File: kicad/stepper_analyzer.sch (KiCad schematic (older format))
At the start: 22 parts, among them J1 Connector_Conn_01x04_Male, J2 Connector_Conn_01x04_Male, M1 Motor, Q1 AO3400A, U1 ACS70331EOLCTR-2P5B3, U2 ACS70331EOLCTR-2P5B3, U3 Pico

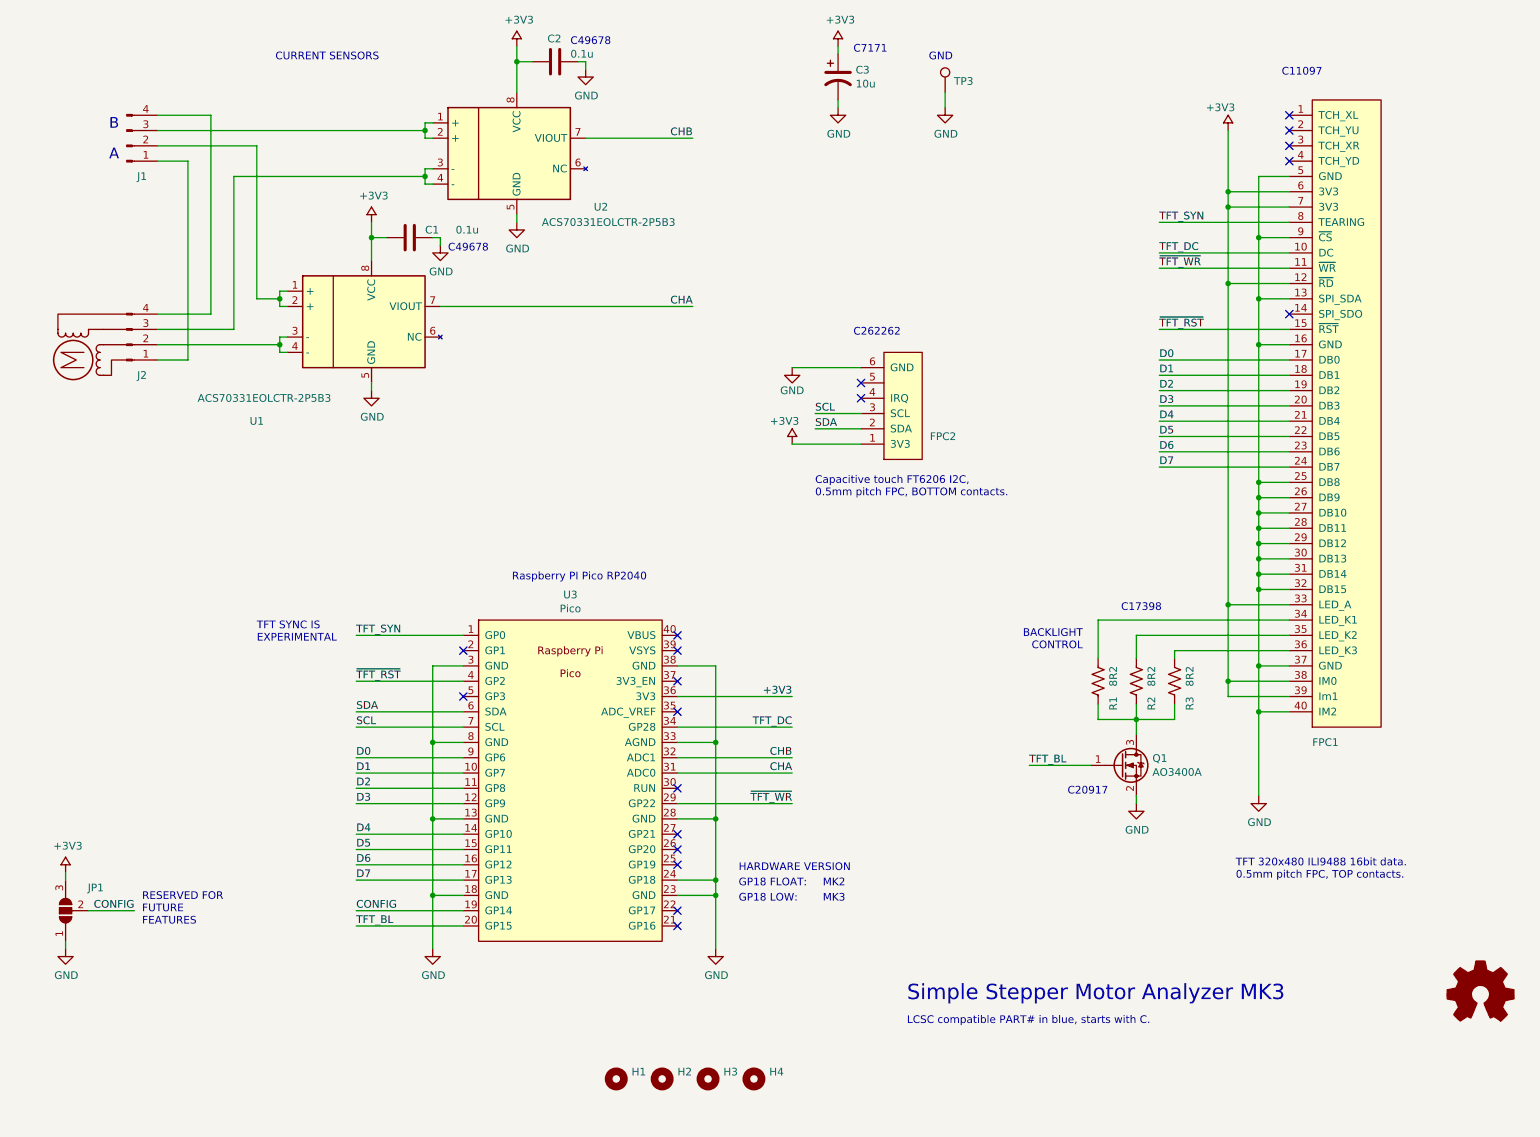
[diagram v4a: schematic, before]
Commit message: Minor schematic tweaks.
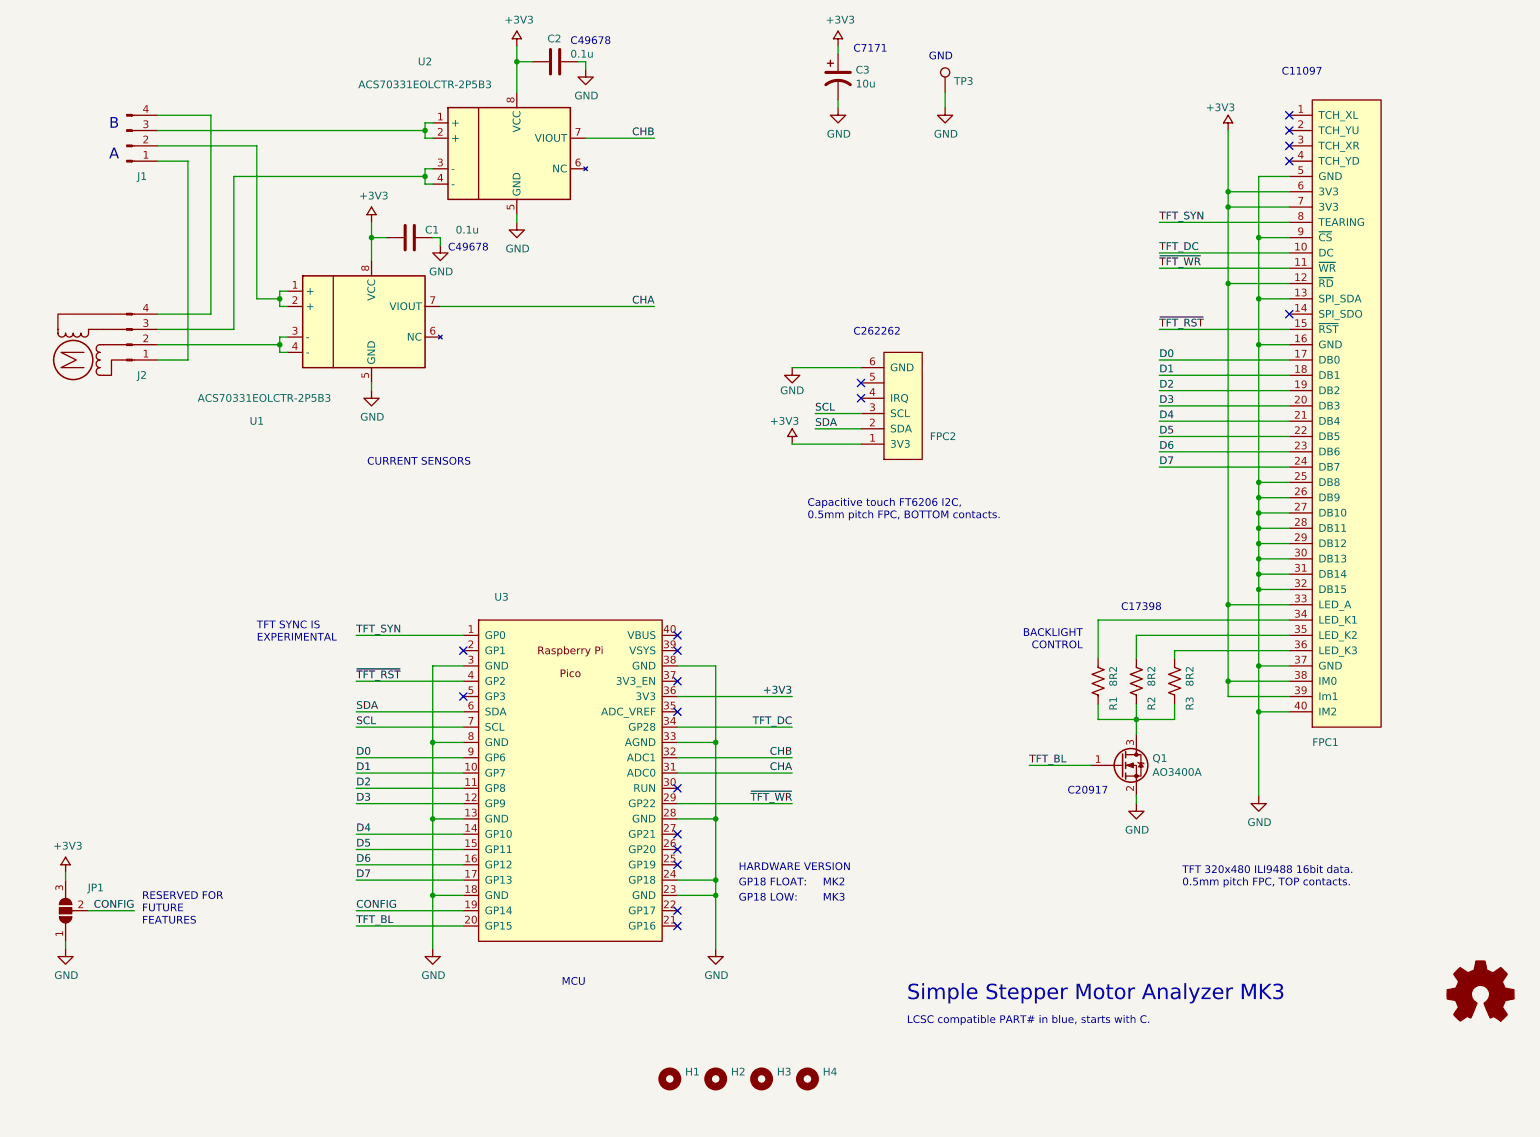
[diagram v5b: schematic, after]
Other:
- note added: "MCU"
- note removed: "Raspberry PI Pico RP2040"
- moved on the sheet: H1, H2, H3, H4
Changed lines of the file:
@@
 U 1 1 609C8FE2
 P 4200 5700
-F 0 "U3" H 4200 6915 50  0000 C CNN
-F 1 "Pico" H 4200 6824 50  0000 C CNN
+F 0 "U3" H 3750 6900 50  0000 C CNN
+F 1 "Pico" H 4200 6824 50  0001 C CNN
 F 2 "stepper_motor_analyzer:Pico_smd_dedicated" V 4200 5700 50  0001 C CNN
 F 3 "" H 4200 5700 50  0001 C CNN
@@
 Wire Wire Line
 	3850 2000 3850 2050
-Text Label 5000 1500 2    50   ~ 0
+Text Label 4750 1500 2    50   ~ 0
 CHB
 Wire Wire Line
@@
 Wire Wire Line
 	1500 1550 2150 1550
-Text Label 5000 2600 2    50   ~ 0
+Text Label 4750 2600 2    50   ~ 0
 CHA
 NoConn ~ 4900 5250
-Text Notes 2950 1000 2    50   ~ 0
+Text Notes 3550 3650 2    50   ~ 0
 CURRENT SENSORS
 $Comp
@@
 $EndComp
 $Comp
-L Mechanical:MountingHole H1
-U 1 1 60A92EA6
-P 4500 7650
-F 0 "H1" H 4600 7696 50  0000 L CNN
-F 1 "MountingHole" H 4600 7605 50  0001 L CNN
-F 2 "MountingHole:MountingHole_2.5mm_Pad_Via" H 4500 7650 50  0001 C CNN
-F 3 "~" H 4500 7650 50  0001 C CNN
-	1    4500 7650
-	1    0    0    -1
-$EndComp
-$Comp
-L Mechanical:MountingHole H2
-U 1 1 60A93F04
-P 4800 7650
-F 0 "H2" H 4900 7696 50  0000 L CNN
-F 1 "MountingHole" H 4900 7605 50  0001 L CNN
-F 2 "MountingHole:MountingHole_2.5mm_Pad_Via" H 4800 7650 50  0001 C CNN
-F 3 "~" H 4800 7650 50  0001 C CNN
-	1    4800 7650
-	1    0    0    -1
-$EndComp
-$Comp
-L Mechanical:MountingHole H3
-U 1 1 60A9417C
-P 5100 7650
-F 0 "H3" H 5200 7696 50  0000 L CNN
-F 1 "MountingHole" H 5200 7605 50  0001 L CNN
-F 2 "MountingHole:MountingHole_2.5mm_Pad_Via" H 5100 7650 50  0001 C CNN
-F 3 "~" H 5100 7650 50  0001 C CNN
-	1    5100 7650
-	1    0    0    -1
-$EndComp
-$Comp
-L Mechanical:MountingHole H4
-U 1 1 60A94418
-P 5400 7650
-F 0 "H4" H 5500 7696 50  0000 L CNN
-F 1 "MountingHole" H 5500 7605 50  0001 L CNN
-F 2 "MountingHole:MountingHole_2.5mm_Pad_Via" H 5400 7650 50  0001 C CNN
-F 3 "~" H 5400 7650 50  0001 C CNN
-	1    5400 7650
-	1    0    0    -1
-$EndComp
-$Comp
 L stepper_motor_analyzer:ACS70331_soic8 U2
 U 1 1 60AEB4AA
 P 3900 1600
-F 0 "U2" H 4400 1250 50  0000 C CNN
-F 1 "ACS70331EOLCTR-2P5B3" H 4450 1150 50  0000 C CNN
+F 0 "U2" H 3250 2200 50  0000 C CNN
+F 1 "ACS70331EOLCTR-2P5B3" H 3250 2050 50  0000 C CNN
 F 2 "stepper_motor_analyzer:SOIC-8_3.9x4.9mm_P1.27mm" H 4300 1550 50  0001 L CIN
 F 3 "" H 3900 1600 50  0001 C CNN
@@
 Text Notes 7550 4850 2    50   ~ 0
 BACKLIGHT\nCONTROL
-Text Notes 8550 6350 0    50   ~ 0
+Text Notes 8200 6400 0    50   ~ 0
 TFT 320x480 ILI9488 16bit data.\n0.5mm pitch FPC, TOP contacts.
-Text Notes 5800 3850 0    50   ~ 0
+Text Notes 5750 4000 0    50   ~ 0
 Capacitive touch FT6206 I2C,\n0.5mm pitch FPC, BOTTOM contacts.
-Text Notes 4700 4400 2    50   ~ 0
-Raspberry PI Pico RP2040
+Text Notes 4300 7050 2    50   ~ 0
+MCU
 $Comp
 L stepper_motor_analyzer:TestPoint TP3
@@
 C20917
 Wire Wire Line
-	4300 1500 5000 1500
-Wire Wire Line
-	3350 2600 5000 2600
+	4300 1500 4750 1500
+Wire Wire Line
+	3350 2600 4750 2600
+$Comp
+L Mechanical:MountingHole H4
+U 1 1 60A94418
+P 5750 7650
+F 0 "H4" H 5850 7696 50  0000 L CNN
+F 1 "MountingHole" H 5850 7605 50  0001 L CNN
+F 2 "MountingHole:MountingHole_2.5mm_Pad_Via" H 5750 7650 50  0001 C CNN
+F 3 "~" H 5750 7650 50  0001 C CNN
+	1    5750 7650
+	1    0    0    -1
+$EndComp
+$Comp
+L Mechanical:MountingHole H3
+U 1 1 60A9417C
+P 5450 7650
+F 0 "H3" H 5550 7696 50  0000 L CNN
+F 1 "MountingHole" H 5550 7605 50  0001 L CNN
+F 2 "MountingHole:MountingHole_2.5mm_Pad_Via" H 5450 7650 50  0001 C CNN
+F 3 "~" H 5450 7650 50  0001 C CNN
+	1    5450 7650
+	1    0    0    -1
+$EndComp
+$Comp
+L Mechanical:MountingHole H2
+U 1 1 60A93F04
+P 5150 7650
+F 0 "H2" H 5250 7696 50  0000 L CNN
+F 1 "MountingHole" H 5250 7605 50  0001 L CNN
+F 2 "MountingHole:MountingHole_2.5mm_Pad_Via" H 5150 7650 50  0001 C CNN
+F 3 "~" H 5150 7650 50  0001 C CNN
+	1    5150 7650
+	1    0    0    -1
+$EndComp
+$Comp
+L Mechanical:MountingHole H1
+U 1 1 60A92EA6
+P 4850 7650
+F 0 "H1" H 4950 7696 50  0000 L CNN
+F 1 "MountingHole" H 4950 7605 50  0001 L CNN
+F 2 "MountingHole:MountingHole_2.5mm_Pad_Via" H 4850 7650 50  0001 C CNN
+F 3 "~" H 4850 7650 50  0001 C CNN
+	1    4850 7650
+	1    0    0    -1
+$EndComp
 $EndSCHEMATC
